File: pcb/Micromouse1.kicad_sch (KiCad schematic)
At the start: 8 parts

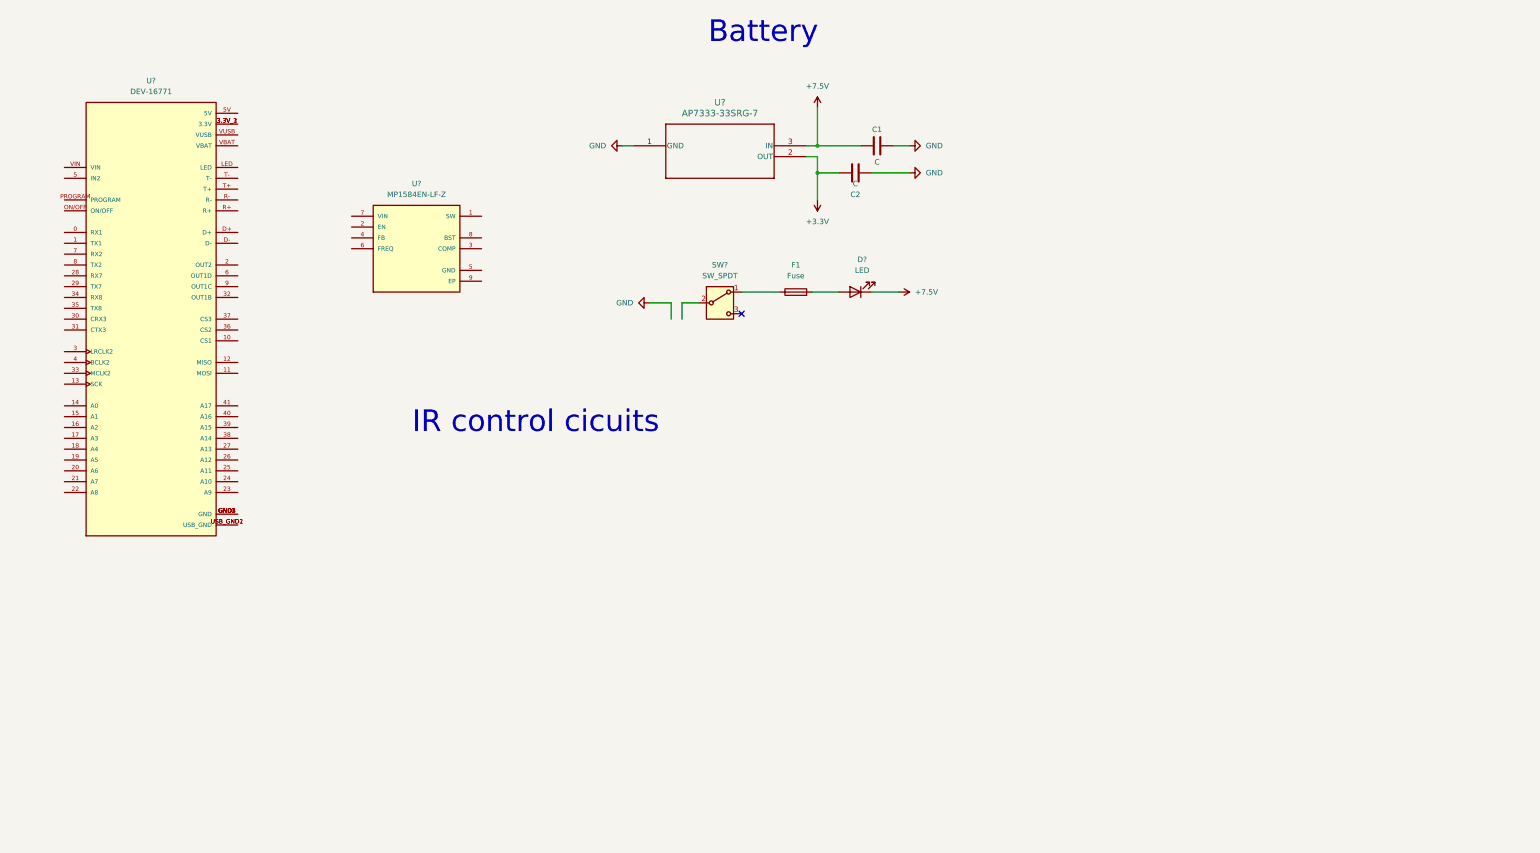
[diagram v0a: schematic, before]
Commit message: added IR module and power module for PCB
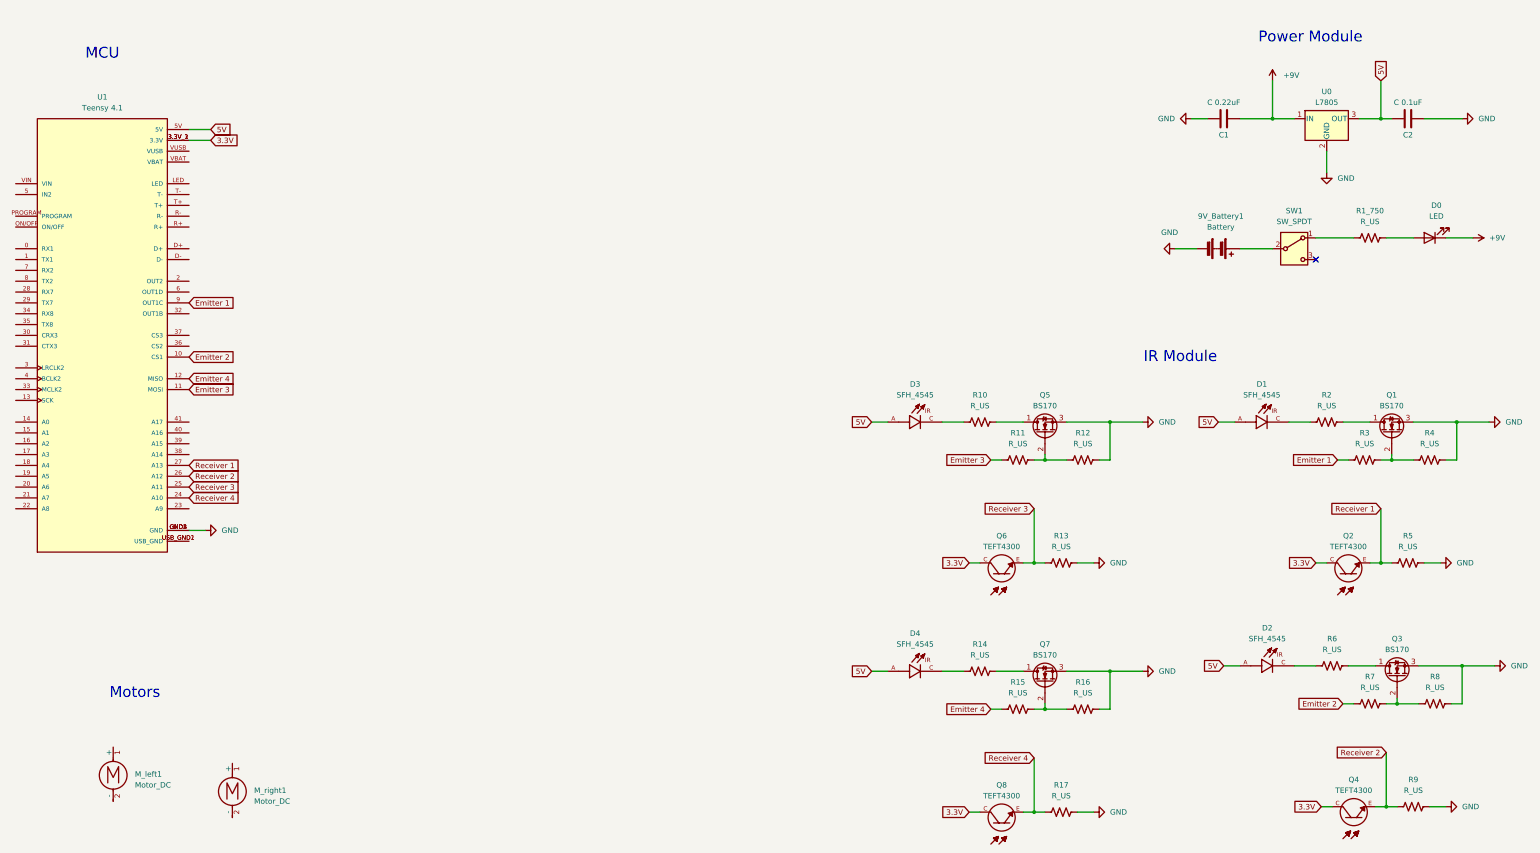
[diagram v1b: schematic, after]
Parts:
- removed F1: Fuse, symbol Device:Fuse
- removed U?: AP7333-33SRG-7, SOT23R_DIO, symbol 2025-10-10_00-09-43:AP7333-33SRG-7
- removed U?: MP1584EN-LF-Z, MP1584EN-LF-Z:SOIC127P600X170-9N, symbol MP1584EN-LF-Z:MP1584EN-LF-Z
- added 9V_Battery1: Battery, symbol Device:Battery
- added D1, D2, D3, D4: SFH_4545, SFH_4545:DIO_SFH_4545, symbol SFH_4545:SFH_4545
- added M_left1, M_right1: Motor_DC, symbol Motor:Motor_DC
- added Q1, Q3, Q5, Q7: BS170, Package_TO_SOT_THT:TO-92_Inline, symbol Transistor_FET:BS170
- added Q2, Q4, Q6, Q8: TEFT4300, TEFT4300:XDCR_TEFT4300, symbol TEFT4300:TEFT4300
- added R10, R11, R12, R13, R14, R15, R16, R17, R1_750, R2, R3, R4, R5, R6, R7, R8, R9: R_US, symbol Device:R_US
- added U0: L7805, symbol Regulator_Linear:L7805
- C1: value C -> C 0.22uF
- C2: value C -> C 0.1uF
- U1: renamed from U?; value DEV-16771 -> Teensy 4.1
- gave numbers to parts that had none: 2
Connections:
- net +3.3V is gone; now on net 5V: C2.1
- net GND: now also U1.GND1 (GND), U1.GND2 (GND), U1.GND3 (GND), U1.GND4 (GND), U1.GND5 (GND), 9V_Battery1.2 (-), Q1.3 (S), Q3.3 (S), Q5.3 (S), Q7.3 (S), R12.2, R13.2, R16.2, R17.2, R4.2, R5.2, R8.2, R9.2, U0.2 (GND)
- net at D0.2 (A): now also R1_750.2
- net at SW1.1 (A): now also R1_750.1
- net at SW1.2 (B): now also 9V_Battery1.1 (+)
- net Emitter 2: now reaches U1.10 (CS1)
- net Emitter 2: now also R7.1
- net Emitter 3: now reaches U1.11 (MOSI)
- net Emitter 3: now also R11.1
- net Emitter 4: now reaches U1.12 (MISO)
- net Emitter 4: now also R15.1
- net Receiver 4: now reaches U1.24 (A10)
- net Receiver 4: now also Q8.E, R17.1
- net Receiver 3: now reaches U1.25 (A11)
- net Receiver 3: now also Q6.E, R13.1
- net Receiver 2: now reaches U1.26 (A12)
- net Receiver 2: now also Q4.E, R9.1
- net Receiver 1: now reaches U1.27 (A13)
- net Receiver 1: now also Q2.E, R5.1
- net 3.3V: now reaches U1.3.3V_1 (3.3V), U1.3.3V_2 (3.3V), U1.3.3V_3 (3.3V)
- net 3.3V: now also Q2.C, Q4.C, Q6.C, Q8.C
- net 5V: now reaches U1.5V
- net 5V: now also D1.A, D2.A, D3.A, D4.A, U0.3 (OUT)
- net Emitter 1: now reaches U1.9 (OUT1C)
- net Emitter 1: now also R3.1
- net +7.5V renamed +9V
- net +9V: now also U0.1 (IN)
- new net: Q5.2 (G), R11.2, R12.1
- new net: D1.C, R2.1
- new net: Q1.1 (D), R2.2
- new net: Q3.2 (G), R7.2, R8.1
- new net: Q7.2 (G), R15.2, R16.1
- new net: D3.C, R10.1
- new net: Q5.1 (D), R10.2
- new net: Q7.1 (D), R14.2
- new net: Q1.2 (G), R3.2, R4.1
- new net: D4.C, R14.1
- new net: D2.C, R6.1
- new net: Q3.1 (D), R6.2
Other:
- note added: "IR Module"
- note added: "MCU"
- note added: "Motors"
- note added: "Power Module"
- note removed: "Battery"
- note removed: "IR control cicuits"
- moved on the sheet: C1, C2, D0, SW1, U1
